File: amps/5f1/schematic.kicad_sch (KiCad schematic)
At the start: 26 parts, among them T2 SE 5k:8

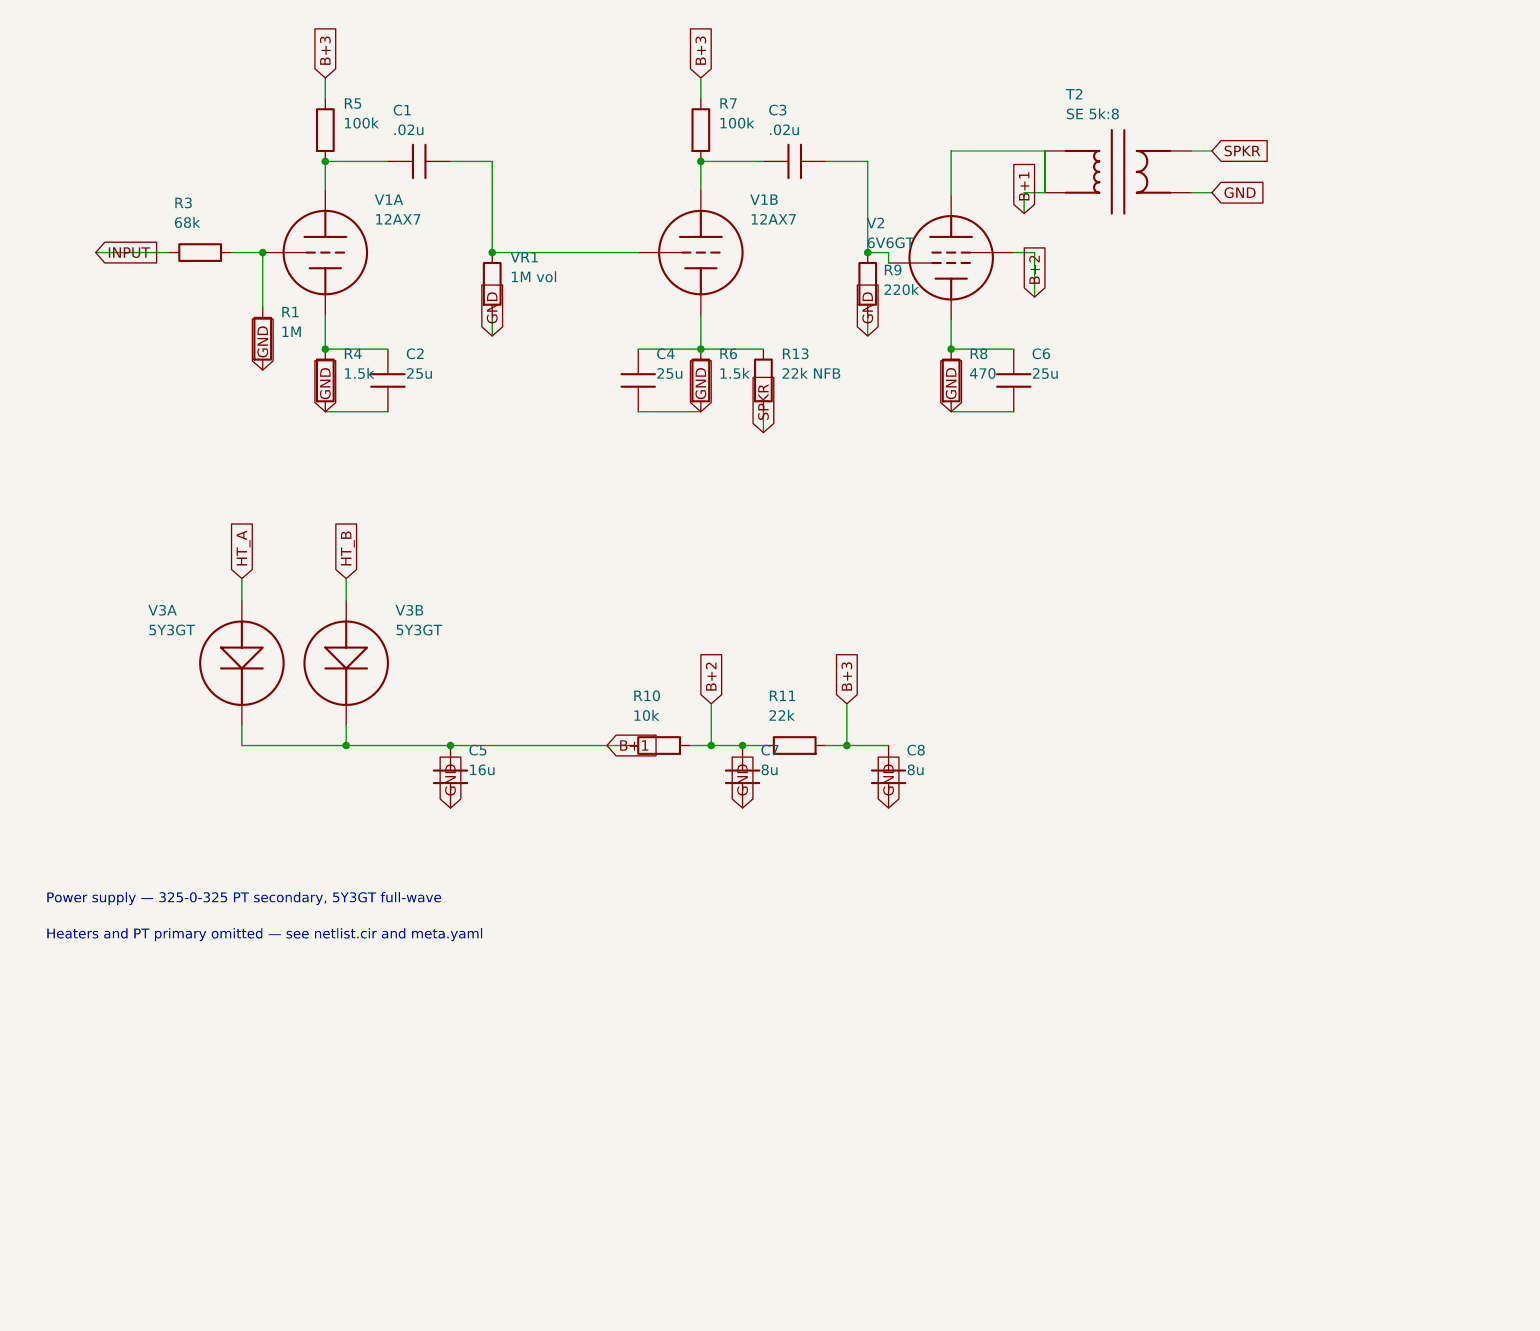
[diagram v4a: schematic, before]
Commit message: Fix: rotated global labels lettered their net names outside the flag
Every global label this pipeline emitted carried (justify left) regardless of
rotation. KiCanvas — like KiCad — draws label text horizontally at 0/180 and
vertically at 90/270 and reads WHICH SIDE of the anchor it letters on from the
justification, so at 180 and 270 the name printed outside an empty flag
outline, struck through by the very wire it names: 219 labels at 180 deg
(including the input-jack flags at top-left of nearly every sheet, the first
glyphs a visitor reads) and 792 GND/rail flags at 270 whose names squeezed at
the flag mouth instead of lettering down the body. The library already
compensated rotation for property text (`pa`); this mirrors that logic for
global labels: justify right at 180/270, left at 0/90.

check_schematics gains the geometry clause whose absence let all 1011
instances through a "no lettering through circuitry" pass: it modelled the
flag box but never the label TEXT, so a name rendered on the wrong side was
invisible to it. The gate now proves justification compensates rotation on
every global label.

Two more things this exposed, fixed in the same engine pass:

- Placement now measures with the renderer's own Newstroke advance table
  (extracted from the vendored kicanvas.js) instead of a flat 0.68-em prose
  average that under-read part lettering by a quarter — the mechanism behind
  every "metered clean, printed through its neighbour" incident. The GATE
  deliberately keeps the coarse ruler: re-ruling it with renderer truth was
  tried and red-flagged 28 of 34 sheets over abutments three visual passes
  had already judged sub-visual (the two-rulers note in schematic_lib.py).
- place_captions' escape ladder runs further, because a banner caption
  measured truly is half again wider than the old estimate believed.

All 34 schematics regenerated; full gate suite green.

🤖 Generated with [Claude Code](https://claude.com/claude-code)

Co-Authored-By: Claude Fable 5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
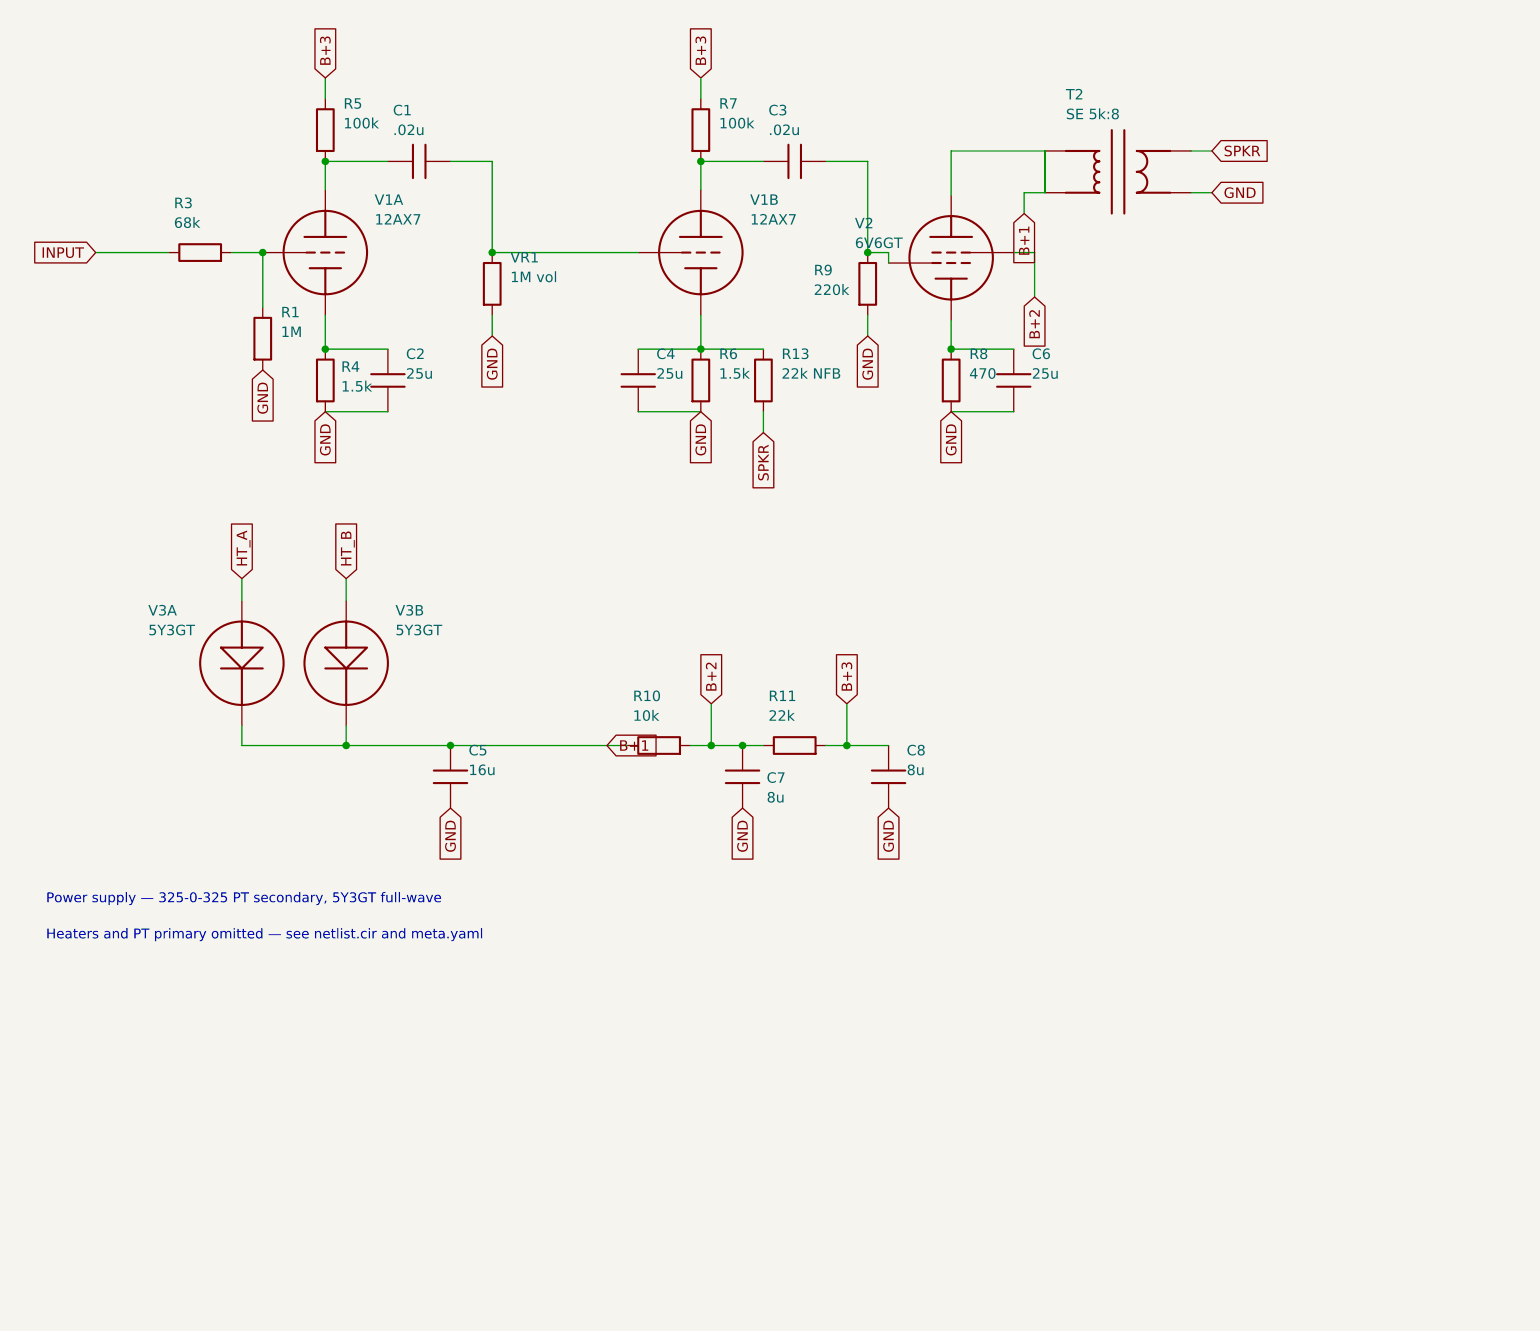
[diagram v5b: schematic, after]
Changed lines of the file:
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@@
     (comment 3 "Values read from: https://robrobinette.com/How_Amps_Work.htm"))
   (global_label "INPUT" (shape input) (at 18.7452 38.278 180)
-    (effects (font (size 1.27 1.27)) (justify left)))
+    (effects (font (size 1.27 1.27)) (justify right)))
   (wire (pts (xy 18.7452 38.278) (xy 27.6552 38.278))
     (stroke (width 0) (type default)))
@@
     (stroke (width 0) (type default)))
   (global_label "GND" (shape input) (at 39.0852 52.578 270)
-    (effects (font (size 1.27 1.27)) (justify left)))
+    (effects (font (size 1.27 1.27)) (justify right)))
   (wire (pts (xy 46.7052 45.898) (xy 46.7052 50.038))
     (stroke (width 0) (type default)))
@@
   (symbol (lib_id "cx:R") (at 46.7052 53.848 0) (unit 1)
     (in_bom yes) (on_board yes)
-    (property "Reference" "R4" (at 48.9052 50.648 0) (effects (font (size 1.27 1.27)) (justify left)))
-    (property "Value" "1.5k" (at 48.9052 53.048 0) (effects (font (size 1.27 1.27)) (justify left))))
+    (property "Reference" "R4" (at 48.6212 52.208 0) (effects (font (size 1.27 1.27)) (justify left)))
+    (property "Value" "1.5k" (at 48.6212 54.608 0) (effects (font (size 1.27 1.27)) (justify left))))
   (wire (pts (xy 46.7052 50.038) (xy 54.3252 50.038))
     (stroke (width 0) (type default)))
@@
     (stroke (width 0) (type default)))
   (global_label "GND" (shape input) (at 46.7052 57.658 270)
-    (effects (font (size 1.27 1.27)) (justify left)))
+    (effects (font (size 1.27 1.27)) (justify right)))
   (wire (pts (xy 46.7052 30.658) (xy 46.7052 27.178))
     (stroke (width 0) (type default)))
@@
     (stroke (width 0) (type default)))
   (global_label "GND" (shape input) (at 67.0252 48.438 270)
-    (effects (font (size 1.27 1.27)) (justify left)))
+    (effects (font (size 1.27 1.27)) (justify right)))
   (wire (pts (xy 67.0252 38.278) (xy 84.8052 38.278))
     (stroke (width 0) (type default)))
@@
     (stroke (width 0) (type default)))
   (global_label "GND" (shape input) (at 92.4252 57.658 270)
-    (effects (font (size 1.27 1.27)) (justify left)))
+    (effects (font (size 1.27 1.27)) (justify right)))
   (wire (pts (xy 92.4252 50.038) (xy 100.045 50.038))
     (stroke (width 0) (type default)))
@@
     (stroke (width 0) (type default)))
   (global_label "SPKR" (shape input) (at 100.045 60.198 270)
-    (effects (font (size 1.27 1.27)) (justify left)))
+    (effects (font (size 1.27 1.27)) (justify right)))
   (wire (pts (xy 92.4252 30.658) (xy 92.4252 27.178))
     (stroke (width 0) (type default)))
@@
   (symbol (lib_id "cx:R") (at 112.745 42.088 0) (unit 1)
     (in_bom yes) (on_board yes)
-    (property "Reference" "R9" (at 114.661 40.448 0) (effects (font (size 1.27 1.27)) (justify left)))
-    (property "Value" "220k" (at 114.661 42.848 0) (effects (font (size 1.27 1.27)) (justify left))))
+    (property "Reference" "R9" (at 106.173 40.448 0) (effects (font (size 1.27 1.27)) (justify left)))
+    (property "Value" "220k" (at 106.173 42.848 0) (effects (font (size 1.27 1.27)) (justify left))))
   (wire (pts (xy 112.745 45.898) (xy 112.745 48.438))
     (stroke (width 0) (type default)))
   (global_label "GND" (shape input) (at 112.745 48.438 270)
-    (effects (font (size 1.27 1.27)) (justify left)))
+    (effects (font (size 1.27 1.27)) (justify right)))
   (wire (pts (xy 112.745 38.278) (xy 115.285 38.278))
     (stroke (width 0) (type default)))
   (symbol (lib_id "cx:PENTODE") (at 122.905 38.913 0) (unit 1)
     (in_bom yes) (on_board yes)
-    (property "Reference" "V2" (at 112.607 34.733 0) (effects (font (size 1.27 1.27)) (justify left)))
-    (property "Value" "6V6GT" (at 112.607 37.133 0) (effects (font (size 1.27 1.27)) (justify left))))
+    (property "Reference" "V2" (at 111.181 34.733 0) (effects (font (size 1.27 1.27)) (justify left)))
+    (property "Value" "6V6GT" (at 111.181 37.133 0) (effects (font (size 1.27 1.27)) (justify left))))
   (wire (pts (xy 115.285 38.278) (xy 115.285 39.548))
     (stroke (width 0) (type default)))
@@
     (stroke (width 0) (type default)))
   (global_label "B+2" (shape input) (at 133.065 43.688 270)
-    (effects (font (size 1.27 1.27)) (justify left)))
+    (effects (font (size 1.27 1.27)) (justify right)))
   (wire (pts (xy 122.905 46.533) (xy 122.905 50.038))
     (stroke (width 0) (type default)))
@@
     (stroke (width 0) (type default)))
   (global_label "GND" (shape input) (at 122.905 57.658 270)
-    (effects (font (size 1.27 1.27)) (justify left)))
+    (effects (font (size 1.27 1.27)) (justify right)))
   (wire (pts (xy 122.905 31.293) (xy 122.905 25.908))
     (stroke (width 0) (type default)))
@@
     (stroke (width 0) (type default)))
   (global_label "B+1" (shape input) (at 131.795 33.528 270)
-    (effects (font (size 1.27 1.27)) (justify left)))
+    (effects (font (size 1.27 1.27)) (justify right)))
   (wire (pts (xy 152.115 25.908) (xy 154.655 25.908))
     (stroke (width 0) (type default)))
@@
     (property "Value" "16u" (at 64.1452 101.308 0) (effects (font (size 1.27 1.27)) (justify left))))
   (global_label "GND" (shape input) (at 61.9452 105.918 270)
-    (effects (font (size 1.27 1.27)) (justify left)))
+    (effects (font (size 1.27 1.27)) (justify right)))
   (global_label "B+1" (shape input) (at 80.9952 98.298 0)
     (effects (font (size 1.27 1.27)) (justify left)))
@@
   (symbol (lib_id "cx:C") (at 97.5052 102.108 0) (unit 1)
     (in_bom yes) (on_board yes)
-    (property "Reference" "C7" (at 99.7052 98.908 0) (effects (font (size 1.27 1.27)) (justify left)))
-    (property "Value" "8u" (at 99.7052 101.308 0) (effects (font (size 1.27 1.27)) (justify left))))
+    (property "Reference" "C7" (at 100.437 102.246 0) (effects (font (size 1.27 1.27)) (justify left)))
+    (property "Value" "8u" (at 100.437 104.646 0) (effects (font (size 1.27 1.27)) (justify left))))
   (global_label "GND" (shape input) (at 97.5052 105.918 270)
-    (effects (font (size 1.27 1.27)) (justify left)))
+    (effects (font (size 1.27 1.27)) (justify right)))
   (symbol (lib_id "cx:R") (at 103.855 98.298 90) (unit 1)
     (in_bom yes) (on_board yes)
@@
     (property "Value" "8u" (at 117.485 101.308 0) (effects (font (size 1.27 1.27)) (justify left))))
   (global_label "GND" (shape input) (at 115.285 105.918 270)
-    (effects (font (size 1.27 1.27)) (justify left)))
+    (effects (font (size 1.27 1.27)) (justify right)))
   (text "Power supply — 325-0-325 PT secondary, 5Y3GT full-wave" (at 12.7 117.076 0)
     (effects (font (size 1.2 1.2)) (justify left)))

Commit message: Fix: deterministic schematic ids and wires split at every join
- _u() is uuid5 over (amp id, emission order), so a regeneration of an
  unchanged script is byte-identical and a drift gate becomes possible
- write() splits wire segments at symbol pins, wire ends and junction dots,
  so the file connects exactly what the drawing shows under KiCad's
  endpoint-only semantics (270 pins were on a wire's interior; net
  partitions unchanged on all 38 sheets)
- all sheets regenerated; aa864-bassman title block was stale (draft) and
  now matches meta.yaml (verified)

Co-Authored-By: Claude Fable 5.1 <noreply@anthropic.com>
Claude-Session: https://claude.ai/code/session_01KBMfdh37HmCL2iWcBiL5J1
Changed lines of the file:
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@@
   (wire (pts (xy 49.2452 95.898) (xy 49.2452 98.298))
     (stroke (width 0) (type default)))
-  (wire (pts (xy 36.5452 98.298) (xy 80.9952 98.298))
+  (wire (pts (xy 36.5452 98.298) (xy 49.2452 98.298))
+    (stroke (width 0) (type default)))
+  (wire (pts (xy 49.2452 98.298) (xy 61.9452 98.298))
+    (stroke (width 0) (type default)))
+  (wire (pts (xy 61.9452 98.298) (xy 80.9952 98.298))
     (stroke (width 0) (type default)))
   (junction (at 49.2452 98.298) (diameter 0) (color 0 0 0 0))
@@
     (property "Reference" "R10" (at 84.1452 92.298 270) (effects (font (size 1.27 1.27)) (justify left)))
     (property "Value" "10k" (at 84.1452 94.698 270) (effects (font (size 1.27 1.27)) (justify left))))
-  (wire (pts (xy 91.1552 98.298) (xy 100.045 98.298))
+  (wire (pts (xy 91.1552 98.298) (xy 93.6952 98.298))
+    (stroke (width 0) (type default)))
+  (wire (pts (xy 93.6952 98.298) (xy 97.5052 98.298))
+    (stroke (width 0) (type default)))
+  (wire (pts (xy 97.5052 98.298) (xy 100.045 98.298))
     (stroke (width 0) (type default)))
   (junction (at 93.6952 98.298) (diameter 0) (color 0 0 0 0))
@@
     (property "Reference" "R11" (at 100.655 92.298 270) (effects (font (size 1.27 1.27)) (justify left)))
     (property "Value" "22k" (at 100.655 94.698 270) (effects (font (size 1.27 1.27)) (justify left))))
-  (wire (pts (xy 107.665 98.298) (xy 115.285 98.298))
+  (wire (pts (xy 107.665 98.298) (xy 110.205 98.298))
+    (stroke (width 0) (type default)))
+  (wire (pts (xy 110.205 98.298) (xy 115.285 98.298))
     (stroke (width 0) (type default)))
   (junction (at 110.205 98.298) (diameter 0) (color 0 0 0 0))
